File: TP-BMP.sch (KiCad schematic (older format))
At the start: 50 parts, among them P1 FPC, P2 JST GH 10-pos, Q1 DMG1024UV-7, Q2 DMG1023UV-7, U1 TLV70233DBV, U2 74LVC2T45, U3 74LVC2T45, U4 74LVC2T45, U5 74LVC2T45, U6 STM32F103CBUx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

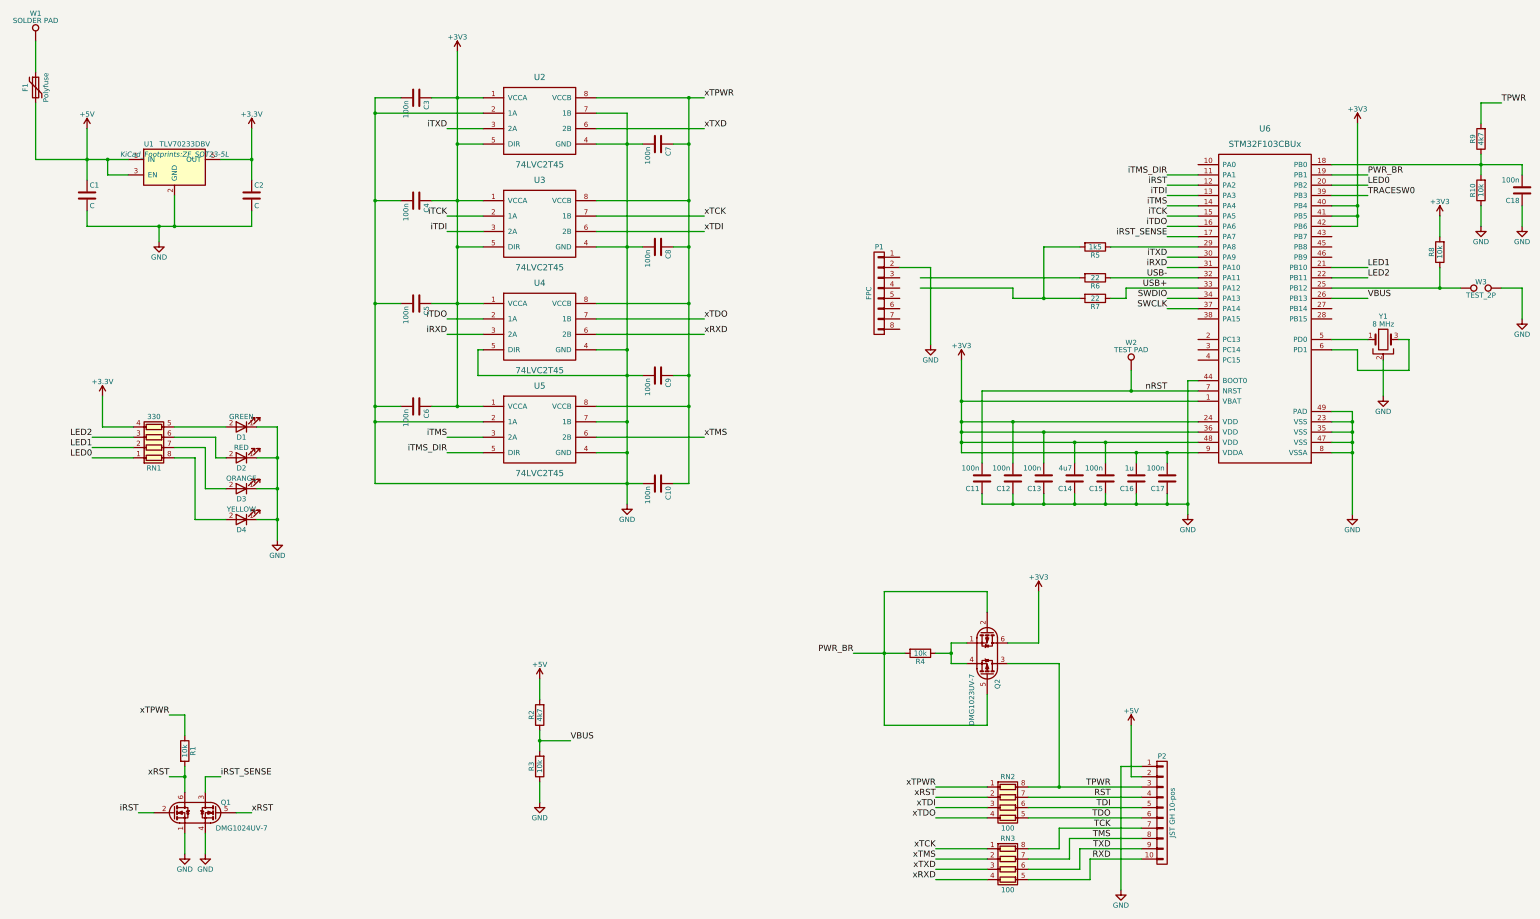
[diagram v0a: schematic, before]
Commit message: Finished rev 0.1 PCB and ordered. Not yet tested. 4-layer design fit-checked with cardboard vs X220. Should be compatible with BMP v2.1.
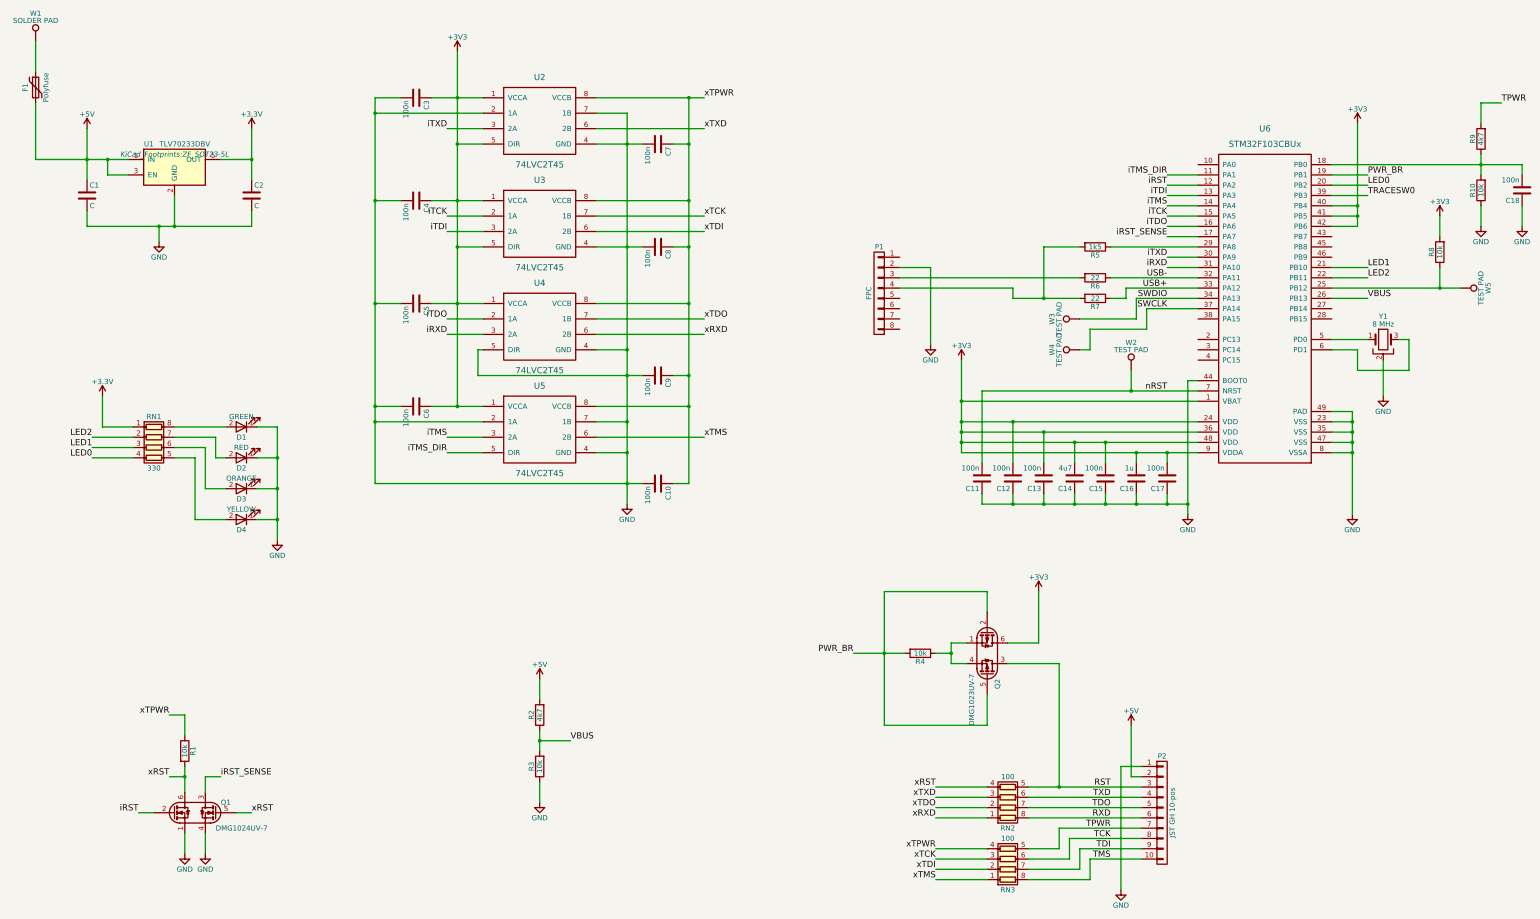
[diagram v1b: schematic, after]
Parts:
- removed W3: TEST_2P, symbol TEST_2P
- added W3, W4, W5: TEST PAD, KiCad_Footprints:ZF_CONN_1-2_pad, symbol TEST_1P
- P1: footprint (none) -> KiCad_Footprints:ZF_CONN_FPC_8POS_52745
- W1: footprint (none) -> KiCad_Footprints:ZF_STRUCT_2.5x1; RoHS (none) -> Yes; Subs Allowed (none) -> No
- W2: footprint (none) -> KiCad_Footprints:ZF_CONN_1-2_pad; RoHS (none) -> Yes; Subs Allowed (none) -> No
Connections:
- net +3V3: now also RN1.1 (R1.1); no longer RN1.4 (R4.1)
- net LED0: now also RN1.4 (R4.1); no longer RN1.1 (R1.1)
- net LED1: now also RN1.3 (R3.1); no longer RN1.2 (R2.1)
- net LED2: now also RN1.2 (R2.1); no longer RN1.3 (R3.1)
- net RST: now also P2.3 (P3), Q2.3, RN2.5 (R4.2); no longer P2.4 (P4), RN2.7 (R2.2)
- net RXD: now also P2.6 (P6), RN2.8 (R1.2); no longer P2.10 (P10), RN3.5 (R4.2)
- net SWCLK: now also W4.1
- net SWDIO: now also W3.1
- net TCK: now also P2.8 (P8), RN3.6 (R3.2); no longer P2.7 (P7), RN3.8 (R1.2)
- net TDI: now also P2.9 (P9), RN3.7 (R2.2); no longer P2.5 (P5), RN2.6 (R3.2)
- net TDO: now also P2.5 (P5), RN2.7 (R2.2); no longer P2.6 (P6), RN2.5 (R4.2)
- net TMS: now also P2.10 (P10), RN3.8 (R1.2); no longer P2.8 (P8), RN3.7 (R2.2)
- net TPWR: now also P2.7 (P7), RN3.5 (R4.2); no longer P2.3 (P3), Q2.3, RN2.8 (R1.2)
- net TXD: now also P2.4 (P4), RN2.6 (R3.2); no longer P2.9 (P9), RN3.6 (R3.2)
- net xRST: now also RN2.4 (R4.1); no longer RN2.2 (R2.1)
- net xRXD: now also RN2.1 (R1.1); no longer RN3.4 (R4.1)
- net xTCK: now also RN3.3 (R3.1); no longer RN3.1 (R1.1)
- net xTDI: now also RN3.2 (R2.1); no longer RN2.3 (R3.1)
- net xTDO: now also RN2.2 (R2.1); no longer RN2.4 (R4.1)
- net xTMS: now also RN3.1 (R1.1); no longer RN3.2 (R2.1)
- net xTPWR: now also RN3.4 (R4.1); no longer RN2.1 (R1.1)
- net xTXD: now also RN2.3 (R3.1); no longer RN3.3 (R3.1)
- net at RN1.5 (R4.2): now also D4.2 (A); no longer D1.2 (A)
- net at RN1.6 (R3.2): now also D3.2 (A); no longer D2.2 (A)
- net at RN1.7 (R2.2): now also D2.2 (A); no longer D3.2 (A)
- net at RN1.8 (R1.2): now also D1.2 (A); no longer D4.2 (A)
- net at R8.1, U6.25 (PB12): now also W5.1
- net at R5.2, R7.2: now also P1.4 (P4)
- net at R6.2: now also P1.3 (P3)
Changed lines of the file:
@@
 L R_Pack04 RN1
 U 1 1 59984FB9
-P 2300 5050
-F 0 "RN1" V 2000 5050 50  0000 C CNN
-F 1 "330" V 2500 5050 50  0000 C CNN
-F 2 "KiCad_Footprints:ZF_RN_4iso_CTS-0804" V 2575 5050 50  0001 C CNN
-F 3 "" H 2300 5050 50  0000 C CNN
-F 4 "No" H 2300 5050 60  0001 C CNN "Subs Allowed"
-F 5 "Yes" H 2300 5050 60  0001 C CNN "RoHS"
-	1    2300 5050
-	0    1    -1   0
+P 2300 5150
+F 0 "RN1" V 2000 5150 50  0000 C CNN
+F 1 "330" V 2500 5150 50  0000 C CNN
+F 2 "KiCad_Footprints:ZF_RN_4iso_CTS-0804" V 2575 5150 50  0001 C CNN
+F 3 "" H 2300 5150 50  0000 C CNN
+F 4 "No" H 2300 5150 60  0001 C CNN "Subs Allowed"
+F 5 "Yes" H 2300 5150 60  0001 C CNN "RoHS"
+	1    2300 5150
+	0    1    1    0
 $EndComp
 $Comp
@@
 L R_Pack04 RN2
 U 1 1 5998AC6E
-P 10600 8650
-F 0 "RN2" V 10300 8650 50  0000 C CNN
-F 1 "100" V 10800 8650 50  0000 C CNN
-F 2 "KiCad_Footprints:ZF_RN_4iso_CTS-0804" V 10875 8650 50  0001 C CNN
-F 3 "" H 10600 8650 50  0000 C CNN
-F 4 "No" H 10600 8650 60  0001 C CNN "Subs Allowed"
-F 5 "Yes" H 10600 8650 60  0001 C CNN "RoHS"
-	1    10600 8650
-	0    1    1    0
+P 10600 8550
+F 0 "RN2" V 10300 8550 50  0000 C CNN
+F 1 "100" V 10800 8550 50  0000 C CNN
+F 2 "KiCad_Footprints:ZF_RN_4iso_CTS-0804" V 10875 8550 50  0001 C CNN
+F 3 "" H 10600 8550 50  0000 C CNN
+F 4 "No" H 10600 8550 60  0001 C CNN "Subs Allowed"
+F 5 "Yes" H 10600 8550 60  0001 C CNN "RoHS"
+	1    10600 8550
+	0    1    -1   0
 $EndComp
 $Comp
 L R_Pack04 RN3
 U 1 1 5998B2B3
-P 10600 9250
-F 0 "RN3" V 10300 9250 50  0000 C CNN
-F 1 "100" V 10800 9250 50  0000 C CNN
-F 2 "KiCad_Footprints:ZF_RN_4iso_CTS-0804" V 10875 9250 50  0001 C CNN
-F 3 "" H 10600 9250 50  0000 C CNN
-F 4 "No" H 10600 9250 60  0001 C CNN "Subs Allowed"
-F 5 "Yes" H 10600 9250 60  0001 C CNN "RoHS"
-	1    10600 9250
-	0    1    1    0
-$EndComp
+P 10600 9150
+F 0 "RN3" V 10300 9150 50  0000 C CNN
+F 1 "100" V 10800 9150 50  0000 C CNN
+F 2 "KiCad_Footprints:ZF_RN_4iso_CTS-0804" V 10875 9150 50  0001 C CNN
+F 3 "" H 10600 9150 50  0000 C CNN
+F 4 "No" H 10600 9150 60  0001 C CNN "Subs Allowed"
+F 5 "Yes" H 10600 9150 60  0001 C CNN "RoHS"
+	1    10600 9150
+	0    1    -1   0
+$EndComp
+Text Label 9900 9050 2    60   ~ 0
+xTPWR
 Text Label 9900 8450 2    60   ~ 0
-xTPWR
+xRST
+Text Label 9900 9250 2    60   ~ 0
+xTDI
+Text Label 9900 8650 2    60   ~ 0
+xTDO
+Text Label 9900 9150 2    60   ~ 0
+xTCK
+Text Label 9900 9350 2    60   ~ 0
+xTMS
 Text Label 9900 8550 2    60   ~ 0
-xRST
-Text Label 9900 8650 2    60   ~ 0
-xTDI
+xTXD
 Text Label 9900 8750 2    60   ~ 0
-xTDO
-Text Label 9900 9050 2    60   ~ 0
-xTCK
-Text Label 9900 9150 2    60   ~ 0
-xTMS
-Text Label 9900 9250 2    60   ~ 0
-xTXD
-Text Label 9900 9350 2    60   ~ 0
 xRXD
+Text Label 11600 8850 2    60   ~ 0
+TPWR
 Text Label 11600 8450 2    60   ~ 0
-TPWR
+RST
+Text Label 11600 9050 2    60   ~ 0
+TDI
+Text Label 11600 8650 2    60   ~ 0
+TDO
+Text Label 11600 8950 2    60   ~ 0
+TCK
+Text Label 11600 9150 2    60   ~ 0
+TMS
 Text Label 11600 8550 2    60   ~ 0
-RST
-Text Label 11600 8650 2    60   ~ 0
-TDI
+TXD
 Text Label 11600 8750 2    60   ~ 0
-TDO
-Text Label 11600 8850 2    60   ~ 0
-TCK
-Text Label 11600 8950 2    60   ~ 0
-TMS
-Text Label 11600 9050 2    60   ~ 0
-TXD
-Text Label 11600 9150 2    60   ~ 0
 RXD
 $Comp
@@
 	11750 3600 12450 3600
 Wire Wire Line
-	12150 3700 12450 3700
-Wire Wire Line
-	12450 3800 12150 3800
+	11850 3700 12450 3700
+Wire Wire Line
+	11950 3800 12450 3800
 Wire Wire Line
 	12350 5800 12350 4500
@@
 F 0 "P1" H 9350 4100 50  0000 C CNN
 F 1 "FPC" V 9450 3650 50  0000 C CNN
-F 2 "" H 9350 3650 50  0001 C CNN
+F 2 "KiCad_Footprints:ZF_CONN_FPC_8POS_52745" H 9350 3650 50  0001 C CNN
 F 3 "" H 9350 3650 50  0000 C CNN
 F 4 "No" H 9350 3650 60  0001 C CNN "Subs Allowed"
@@
 $EndComp
 Wire Wire Line
-	10650 3700 10650 3600
+	10650 3600 10650 3700
 Connection ~ 10950 3700
 $Comp
@@
 	9850 3400 9550 3400
 Wire Wire Line
-	11300 3500 9750 3500
-Wire Wire Line
-	10650 3600 9750 3600
+	9550 3500 11300 3500
+Wire Wire Line
+	9550 3600 10650 3600
 $Comp
 L +5V #PWR017
@@
 F 0 "W1" H 1150 1470 50  0000 C CNN
 F 1 "SOLDER PAD" H 1150 1400 50  0000 C CNN
-F 2 "" H 1350 1200 50  0001 C CNN
+F 2 "KiCad_Footprints:ZF_STRUCT_2.5x1" H 1350 1200 50  0001 C CNN
 F 3 "" H 1350 1200 50  0000 C CNN
+F 4 "No" H 1150 1200 60  0001 C CNN "Subs Allowed"
+F 5 "Yes" H 1150 1200 60  0001 C CNN "RoHS"
 	1    1150 1200
 	1    0    0    -1
@@
 F 0 "W2" H 11800 4670 50  0000 C CNN
 F 1 "TEST PAD" H 11800 4600 50  0000 C CNN
-F 2 "" H 12000 4400 50  0001 C CNN
+F 2 "KiCad_Footprints:ZF_CONN_1-2_pad" H 12000 4400 50  0001 C CNN
 F 3 "" H 12000 4400 50  0000 C CNN
+F 4 "No" H 11800 4400 60  0001 C CNN "Subs Allowed"
+F 5 "Yes" H 11800 4400 60  0001 C CNN "RoHS"
 	1    11800 4400
 	1    0    0    -1
@@
 Wire Wire Line
 	14800 2900 14800 3100
-$Comp
-L TEST_2P W3
-U 1 1 5999C2C0
-P 15200 3600
-F 0 "W3" H 15200 3660 50  0000 C CNN
-F 1 "TEST_2P" H 15200 3530 50  0000 C CNN
-F 2 "" H 15200 3600 50  0001 C CNN
-F 3 "" H 15200 3600 50  0000 C CNN
-	1    15200 3600
-	1    0    0    -1
-$EndComp
 Connection ~ 14800 3600
-$Comp
-L GND #PWR021
-U 1 1 5999C472
-P 15600 3900
-F 0 "#PWR021" H 15600 3650 50  0001 C CNN
-F 1 "GND" H 15600 3750 50  0000 C CNN
-F 2 "" H 15600 3900 50  0000 C CNN
-F 3 "" H 15600 3900 50  0000 C CNN
-	1    15600 3900
-	1    0    0    -1
-$EndComp
-Wire Wire Line
-	15600 3900 15600 3600
-Wire Wire Line
-	15600 3600 15400 3600
 Text Label 14100 3400 0    60   ~ 0
 LED1
@@
 Connection ~ 14000 2900
 $Comp
-L +3V3 #PWR022
+L +3V3 #PWR021
 U 1 1 5999D237
 P 14000 2000
-F 0 "#PWR022" H 14000 1850 50  0001 C CNN
+F 0 "#PWR021" H 14000 1850 50  0001 C CNN
 F 1 "+3V3" H 14000 2140 50  0000 C CNN
 F 2 "" H 14000 2000 50  0000 C CNN
@@
 Connection ~ 15200 2400
 $Comp
-L GND #PWR023
+L GND #PWR022
 U 1 1 5999DFFD
 P 15200 3000
-F 0 "#PWR023" H 15200 2750 50  0001 C CNN
+F 0 "#PWR022" H 15200 2750 50  0001 C CNN
 F 1 "GND" H 15200 2850 50  0000 C CNN
 F 2 "" H 15200 3000 50  0000 C CNN
@@
 	15200 3000 15200 2800
 $Comp
-L GND #PWR024
+L GND #PWR023
 U 1 1 5999E1EA
 P 15600 3000
-F 0 "#PWR024" H 15600 2750 50  0001 C CNN
+F 0 "#PWR023" H 15600 2750 50  0001 C CNN
 F 1 "GND" H 15600 2850 50  0000 C CNN
 F 2 "" H 15600 3000 50  0000 C CNN
@@
 Wire Wire Line
 	15600 2800 15600 3000
+$Comp
+L TEST_1P W4
+U 1 1 599CE811
+P 11300 4200
+F 0 "W4" H 11300 4470 50  0000 C CNN
+F 1 "TEST PAD" H 11300 4400 50  0000 C CNN
+F 2 "KiCad_Footprints:ZF_CONN_1-2_pad" H 11500 4200 50  0001 C CNN
+F 3 "" H 11500 4200 50  0000 C CNN
+F 4 "No" H 11300 4200 60  0001 C CNN "Subs Allowed"
+F 5 "Yes" H 11300 4200 60  0001 C CNN "RoHS"
+	1    11300 4200
+	0    -1   -1   0
+$EndComp
+$Comp
+L TEST_1P W3
+U 1 1 599CE93D
+P 11300 3900
+F 0 "W3" H 11300 4170 50  0000 C CNN
+F 1 "TEST PAD" H 11300 4100 50  0000 C CNN
+F 2 "KiCad_Footprints:ZF_CONN_1-2_pad" H 11500 3900 50  0001 C CNN
+F 3 "" H 11500 3900 50  0000 C CNN
+F 4 "No" H 11300 3900 60  0001 C CNN "Subs Allowed"
+F 5 "Yes" H 11300 3900 60  0001 C CNN "RoHS"
+	1    11300 3900
+	0    -1   -1   0
+$EndComp
+Wire Wire Line
+	11300 3900 11850 3900
+Wire Wire Line
+	11850 3900 11850 3700
+Wire Wire Line
+	11950 3800 11950 4000
+Wire Wire Line
+	11950 4000 11400 4000
+Wire Wire Line
+	11400 4000 11400 4200
+Wire Wire Line
+	11400 4200 11300 4200
+$Comp
+L TEST_1P W5
+U 1 1 599CEFC2
+P 15000 3600
+F 0 "W5" H 15000 3870 50  0000 C CNN
+F 1 "TEST PAD" H 15000 3800 50  0000 C CNN
+F 2 "KiCad_Footprints:ZF_CONN_1-2_pad" H 15200 3600 50  0001 C CNN
+F 3 "" H 15200 3600 50  0000 C CNN
+F 4 "No" H 15000 3600 60  0001 C CNN "Subs Allowed"
+F 5 "Yes" H 15000 3600 60  0001 C CNN "RoHS"
+	1    15000 3600
+	0    1    1    0
+$EndComp
 $EndSCHEMATC
